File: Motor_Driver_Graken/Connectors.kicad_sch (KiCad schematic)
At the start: 32 parts, among them J1 RC_PWM, J10 Conn_01x02, J11 Conn_01x02, J2 THROTTLE, J3 BREAK, J4 USB_A, J5 SWD, J6 SERIAL, J7 CAN, J8 MOTOR_SENSOR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

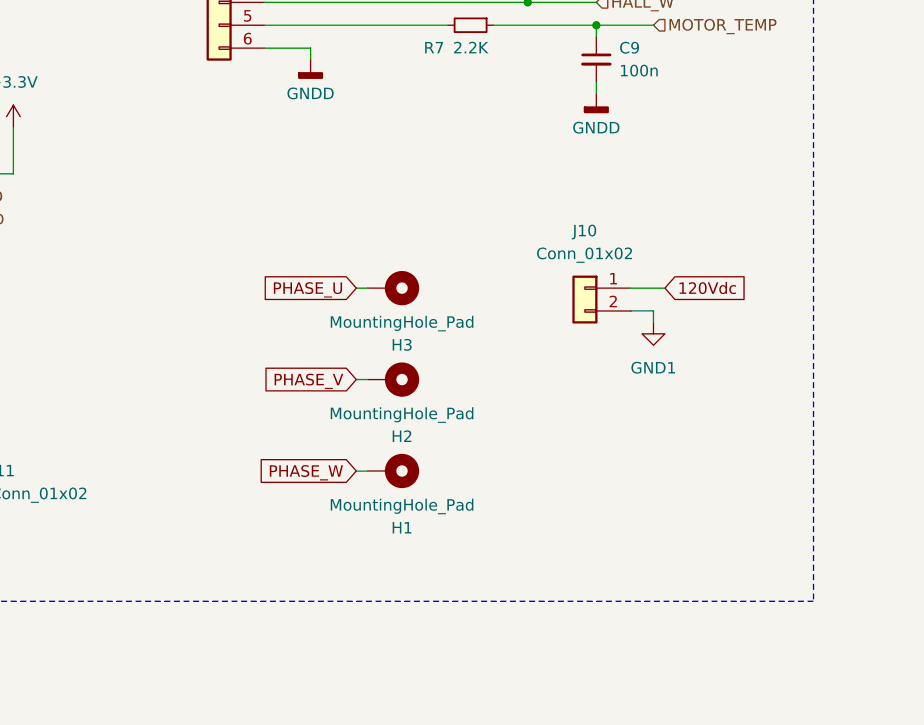
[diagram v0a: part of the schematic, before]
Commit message: adding Simulation Files
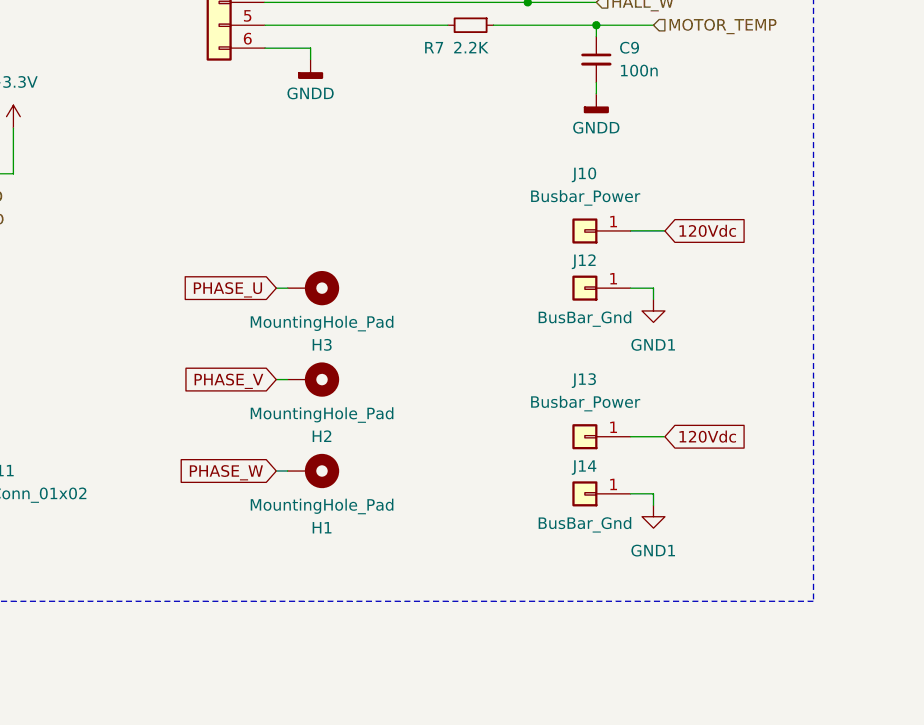
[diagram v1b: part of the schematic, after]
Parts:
- removed J10: Conn_01x02, symbol Connector_Generic:Conn_01x02
- added J10, J13: Busbar_Power, symbol Connector_Generic:Conn_01x01
- added J12, J14: BusBar_Gnd, symbol Connector_Generic:Conn_01x01
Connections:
- net 120Vdc: now also J10.1 (Pin_1), J13.1 (Pin_1)
- net GND1: now also J12.1 (Pin_1), J14.1 (Pin_1)
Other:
- moved on the sheet: H1, H2, H3
